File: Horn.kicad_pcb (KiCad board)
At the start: 2 copper layers, 11 parts, among them J1 USB_C_Receptacle, SW1 Boot, SW2 Enable, U1 AP62300TWU, U2 AP2112K-3.3, Y1 Crystal

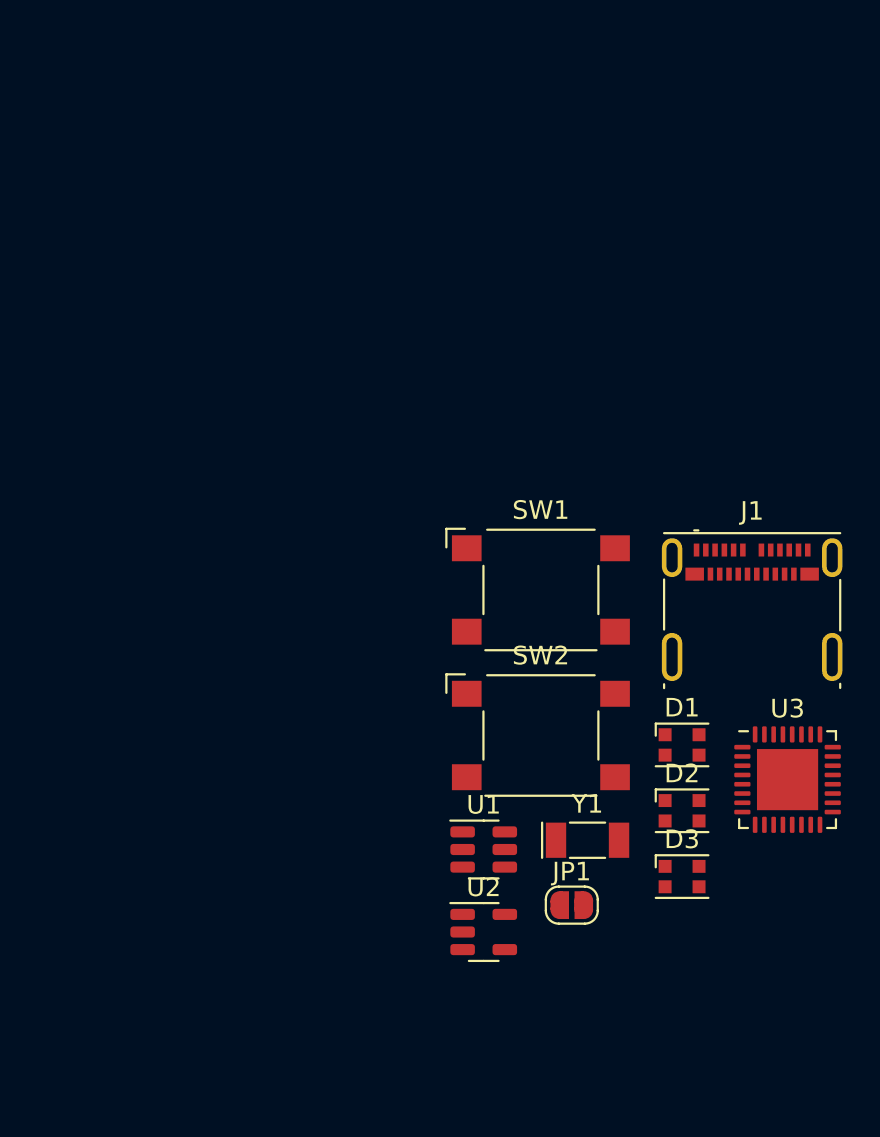
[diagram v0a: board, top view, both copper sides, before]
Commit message: Chose component sizes
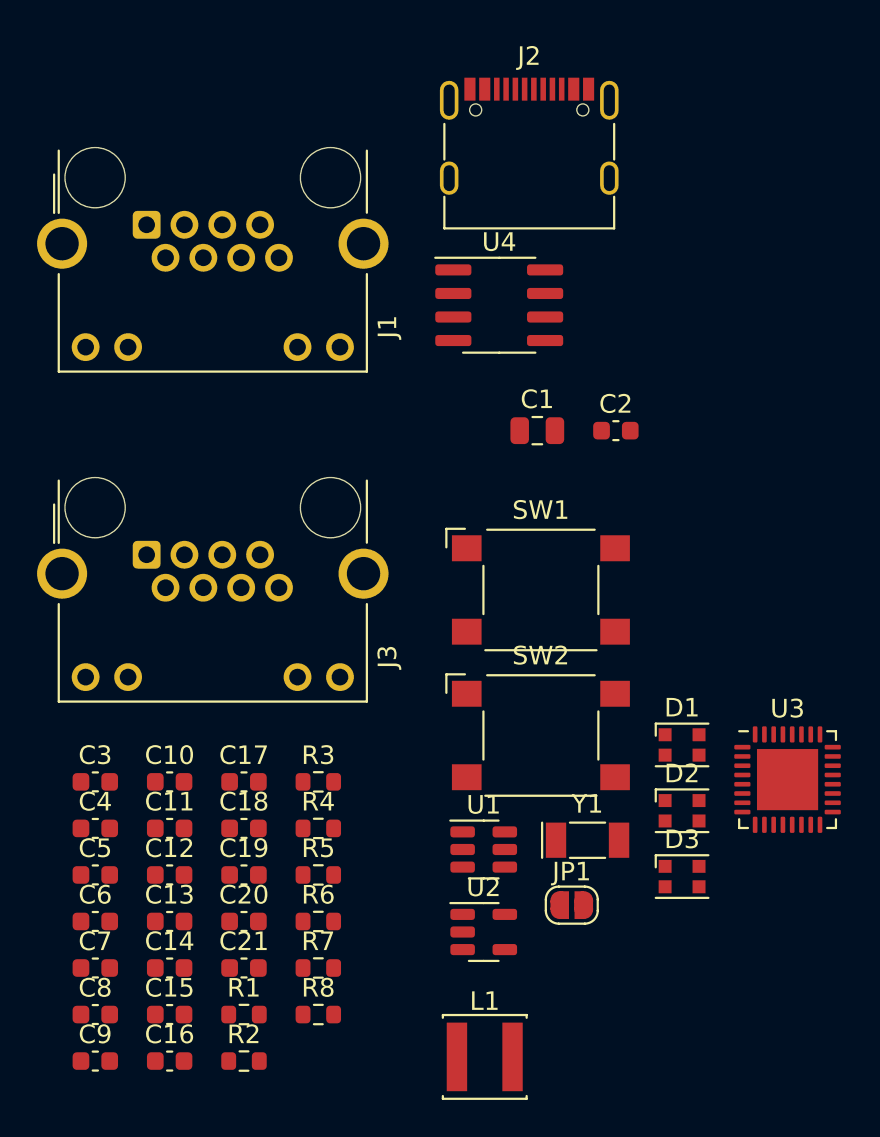
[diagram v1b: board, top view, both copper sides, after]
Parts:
- added C1: 10uF, Capacitor_SMD:C_0805_2012Metric, F.Cu at (148.7, 73.2)
- added C10: 16pF, Capacitor_SMD:C_0603_1608Metric, F.Cu at (128.8, 92.1)
- added C11: 100nF, Capacitor_SMD:C_0603_1608Metric, F.Cu at (128.8, 94.6)
- added C12: 100nF, Capacitor_SMD:C_0603_1608Metric, F.Cu at (128.8, 97.1)
- added C13: 100nF, Capacitor_SMD:C_0603_1608Metric, F.Cu at (128.8, 99.6)
- added C14: 100nF, Capacitor_SMD:C_0603_1608Metric, F.Cu at (128.8, 102.1)
- added C15: 1uF, Capacitor_SMD:C_0603_1608Metric, F.Cu at (128.8, 104.6)
- added C16: 10uF, Capacitor_SMD:C_0603_1608Metric, F.Cu at (128.8, 107.2)
- added C17: 100nF, Capacitor_SMD:C_0603_1608Metric, F.Cu at (132.8, 92.1)
- added C18: 10uF, Capacitor_SMD:C_0603_1608Metric, F.Cu at (132.8, 94.6)
- added C19: 1uF, Capacitor_SMD:C_0603_1608Metric, F.Cu at (132.8, 97.1)
- added C2: 100nF, Capacitor_SMD:C_0603_1608Metric, F.Cu at (152.9, 73.2)
- added C20: 10uF, Capacitor_SMD:C_0603_1608Metric, F.Cu at (132.8, 99.6)
- added C21: 1uF, Capacitor_SMD:C_0603_1608Metric, F.Cu at (132.8, 102.1)
- added C3: 22uF, Capacitor_SMD:C_0603_1608Metric, F.Cu at (124.8, 92.1)
- added C4: 22uF, Capacitor_SMD:C_0603_1608Metric, F.Cu at (124.8, 94.6)
- added C5: 1uF, Capacitor_SMD:C_0603_1608Metric, F.Cu at (124.8, 97.1)
- added C6: 1uF, Capacitor_SMD:C_0603_1608Metric, F.Cu at (124.8, 99.6)
- added C7: 22uF, Capacitor_SMD:C_0603_1608Metric, F.Cu at (124.8, 102.1)
- added C8: 1uF, Capacitor_SMD:C_0603_1608Metric, F.Cu at (124.8, 104.6)
- added C9: 16pF, Capacitor_SMD:C_0603_1608Metric, F.Cu at (124.8, 107.2)
- added J2: USB_C_Receptacle_USB2.0, Connector_USB:USB_C_Receptacle_G-Switch_GT-USB-7010ASV, F.Cu at (148.2, 58.5)
- added J3: RJ45_LED_Shielded, Connector_RJ:RJ45_Connfly_DS1128-09-S8xx-S_Horizontal, F.Cu at (127.6, 79.8)
- added L1: 3.3uH, Inductor_SMD:L_Sunlord_SWPA4030S, F.Cu at (145.8, 106.9)
- added R1: 56.2k, Resistor_SMD:R_0603_1608Metric, F.Cu at (132.8, 104.6)
- added R2: 10k, Resistor_SMD:R_0603_1608Metric, F.Cu at (132.8, 107.2)
- added R3: 10k, Resistor_SMD:R_0603_1608Metric, F.Cu at (136.8, 92.1)
- added R4: 10k, Resistor_SMD:R_0603_1608Metric, F.Cu at (136.8, 94.6)
- added R5: 10k, Resistor_SMD:R_0603_1608Metric, F.Cu at (136.8, 97.1)
- added R6: 0, Resistor_SMD:R_0603_1608Metric, F.Cu at (136.8, 99.6)
- added R7: 10k, Resistor_SMD:R_0603_1608Metric, F.Cu at (136.8, 102.1)
- added R8: 10k, Resistor_SMD:R_0603_1608Metric, F.Cu at (136.8, 104.6)
- added U4: TJA1042T-3, Package_SO:SOIC-8_3.9x4.9mm_P1.27mm, F.Cu at (146.6, 66.4)
- J1: value USB_C_Receptacle -> RJ45_LED_Shielded; footprint Connector_USB:USB_C_Receptacle_Molex_105450-0101 -> Connector_RJ:RJ45_Connfly_DS1128-09-S8xx-S_Horizontal
- moved J1 38.7 mm to (127.6, 62.0)
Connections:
- D1 pad 1: unconnected-(D1-VDD-Pad1) -> +5V
- D2 pad 1: unconnected-(D2-VDD-Pad1) -> +5V
- D3 pad 1: unconnected-(D3-VDD-Pad1) -> +5V
- U3 pad 10: unconnected-(U3-MTDI-Pad10) -> /CAN_RX
- U3 pad 33: unconnected-(U3-GND-Pad33) -> GND
- U3 pad 9: unconnected-(U3-MTMS-Pad9) -> /CAN_TX

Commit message: Started PCB
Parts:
- added J4: Screw_Terminal_01x02, TerminalBlock_MetzConnect:TerminalBlock_MetzConnect_Type011_RT05502HBWC_1x02_P5.00mm_Horizontal, F.Cu at (163.4, 60.7)
- C3, C4, C7: footprint Capacitor_SMD:C_0603_1608Metric -> Capacitor_SMD:C_0805_2012Metric
- moved C10 62.5 mm to (190.6, 101.7)
- moved C11 62.5 mm to (190.6, 104.2)
- moved C12 62.5 mm to (190.6, 106.7)
- moved C13 62.5 mm to (190.6, 109.2)
- moved C14 62.5 mm to (190.6, 111.7)
- moved C15 62.5 mm to (190.6, 114.2)
- moved C16 62.5 mm to (190.6, 116.8)
- moved C17 62.5 mm to (194.6, 101.7)
- moved R3 62.5 mm to (198.6, 101.7)
- moved R4 62.5 mm to (198.6, 104.2)
- moved R5 62.5 mm to (198.6, 106.7)
- moved R6 62.5 mm to (198.6, 109.2)
- moved R7 62.5 mm to (198.6, 111.7)
- moved R8 62.5 mm to (198.6, 114.2)
- moved C8 62.5 mm to (186.6, 114.2)
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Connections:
- C2 pad 1: Net-(U1-SW) -> Net-(U1-BST)
- C2 pad 2: Net-(U1-BST) -> Net-(U1-SW)
- J1 pad 1: unconnected-(J1-Pad1) -> GND
- J1 pad 2: unconnected-(J1-Pad2) -> /CANL
- J1 pad 3: unconnected-(J1-Pad3) -> /CANH
- J1 pad 8: unconnected-(J1-Pad8) -> +5V
- J3 pad 1: unconnected-(J3-Pad1) -> GND
- J3 pad 2: unconnected-(J3-Pad2) -> /CANL
- J3 pad 3: unconnected-(J3-Pad3) -> /CANH
- J3 pad 8: unconnected-(J3-Pad8) -> +5V
- L1 pad 1: Net-(U1-BST) -> Net-(U1-SW)
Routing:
- net Net-(JP1-A): track 0.00 -> 15.8 mm, vias 0 -> 2
- net Net-(U1-SW): track 0.00 -> 8.15 mm
- net GND: track 0.00 -> 6.61 mm
- net Net-(U1-FB): track 0.00 -> 3.96 mm
- net +12V: track 0.00 -> 3.28 mm
- net Net-(U1-BST): track 0.00 -> 2.14 mm
